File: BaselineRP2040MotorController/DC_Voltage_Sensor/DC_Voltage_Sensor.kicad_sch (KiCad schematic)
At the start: 7 parts, among them U16 ADS7822U

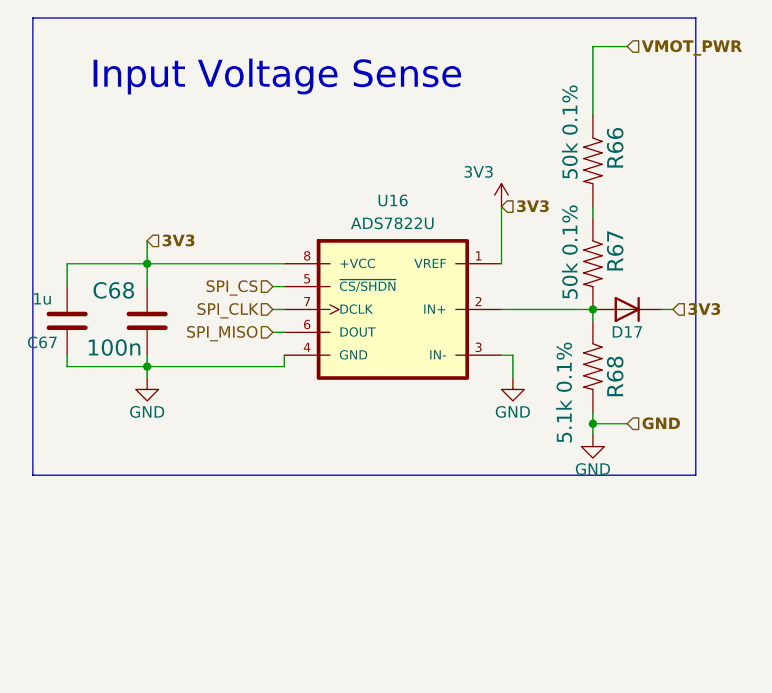
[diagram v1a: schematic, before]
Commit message: Drop some features.
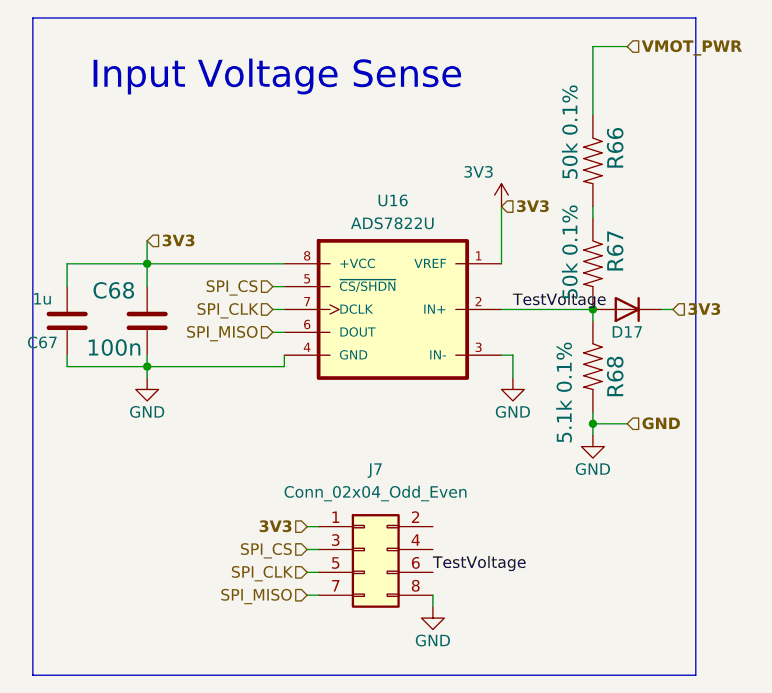
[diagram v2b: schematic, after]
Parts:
- added J7: Conn_02x04_Odd_Even, Connector_PinHeader_1.27mm:PinHeader_2x04_P1.27mm_Vertical, symbol Connector_Generic:Conn_02x04_Odd_Even
- U16: footprint parts:SOIC127P599X175-8N -> Package_TO_SOT_SMD:SuperSOT-8
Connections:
- net 3V3: now also J7.1 (Pin_1)
- net GND: now also J7.8 (Pin_8)
- net SPI_CLK: now also J7.5 (Pin_5)
- net SPI_CS: now also J7.3 (Pin_3)
- net SPI_MISO: now also J7.7 (Pin_7)
- net TestVoltage: now reaches D17.2 (A), R67.2, R68.1, U16.2 (IN+)
- net TestVoltage: now also J7.6 (Pin_6)
